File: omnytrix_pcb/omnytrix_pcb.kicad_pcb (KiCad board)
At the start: 2 copper layers, 38 x 45.5 mm, 17 parts, among them U1 LD3985M33R_SOT23, U3 STM32F411RCTx

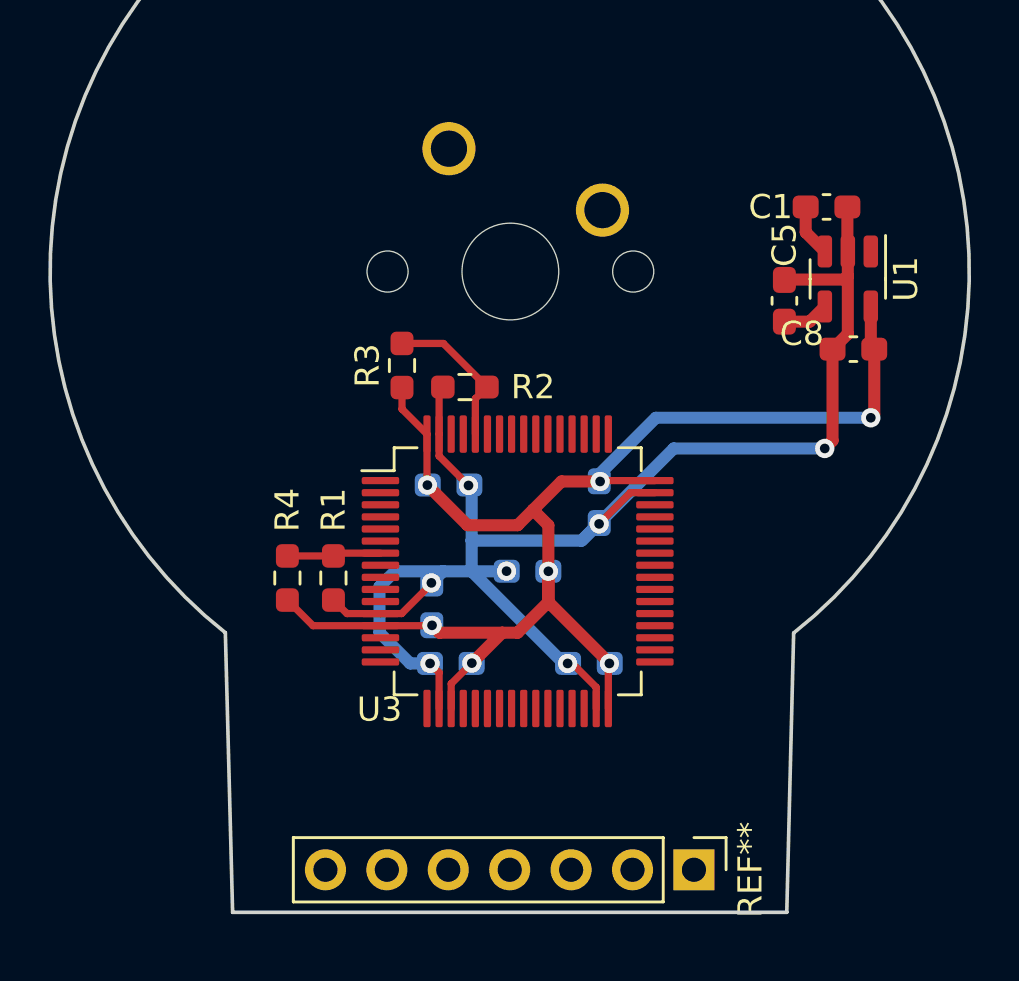
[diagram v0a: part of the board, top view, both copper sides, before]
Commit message: add some R and change position of components
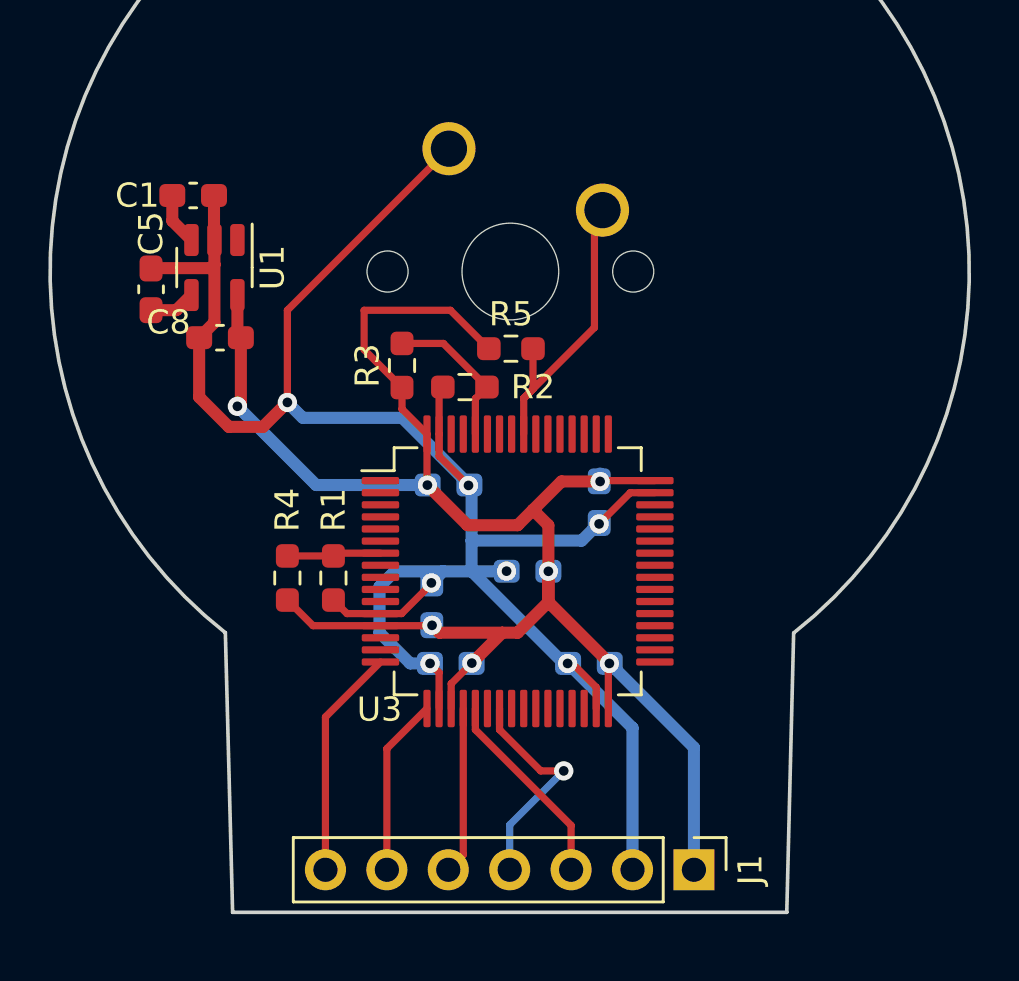
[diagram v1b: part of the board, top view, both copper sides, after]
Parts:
- removed REF**: PinHeader_1x07_P2.54mm_Vertical, Connector_PinHeader_2.54mm:PinHeader_1x07_P2.54mm_Vertical
- removed REF**: SW_Cherry_MX_1.00u_PCB, Button_Switch_Keyboard:SW_Cherry_MX_1.00u_PCB
- added J1: Conn_01x07, Connector_PinHeader_2.54mm:PinHeader_1x07_P2.54mm_Vertical, F.Cu at (107.6, 124.7)
- added R5: 10k, Resistor_SMD:R_0603_1608Metric_Pad0.98x0.95mm_HandSolder, F.Cu at (100.1, 103.2)
- added SW1: SW_Push, Button_Switch_Keyboard:SW_Cherry_MX_1.00u_PCB, B.Cu at (97.5, 94.9)
- moved C1 26.2 mm to (86.9, 96.9)
- moved C5 26.2 mm to (85.2, 100.7)
- moved C8 26.2 mm to (88.0, 102.7)
- moved U1 26.2 mm to (87.8, 99.8)
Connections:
- U3 pad 16: unconnected-(U3-PA2-Pad16) -> /RST
- U3 pad 17: unconnected-(U3-PA3-Pad17) -> /CS
- U3 pad 20: unconnected-(U3-PA4-Pad20) -> /DC
- U3 pad 21: unconnected-(U3-PA5-Pad21) -> /SCL
- U3 pad 23: unconnected-(U3-PA7-Pad23) -> /SDA
- U3 pad 36: unconnected-(U3-PB15-Pad36) -> /SD_CK
- U3 pad 39: unconnected-(U3-PC8-Pad39) -> /SD_D0
- U3 pad 40: unconnected-(U3-PC9-Pad40) -> /SD_D1
- U3 pad 42: unconnected-(U3-PA9-Pad42) -> /SD_D2
- U3 pad 52: unconnected-(U3-PC11-Pad52) -> /SD_D3
- U3 pad 54: unconnected-(U3-PD2-Pad54) -> /SD_CMD
- U3 pad 56: unconnected-(U3-PB4-Pad56) -> /BTN
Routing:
- net GND: track 67.0 -> 90.0 mm
- net +3.3V: track 59.2 -> 75.9 mm
- net /BTN: track 0.00 -> 12.9 mm
- net /RST: track 0.00 -> 9.54 mm
- net /SDA: track 0.00 -> 9.25 mm, vias 0 -> 1
- net /SCL: track 0.00 -> 8.31 mm
- net /CS: track 0.00 -> 7.36 mm
- net /DC: track 0.00 -> 6.93 mm

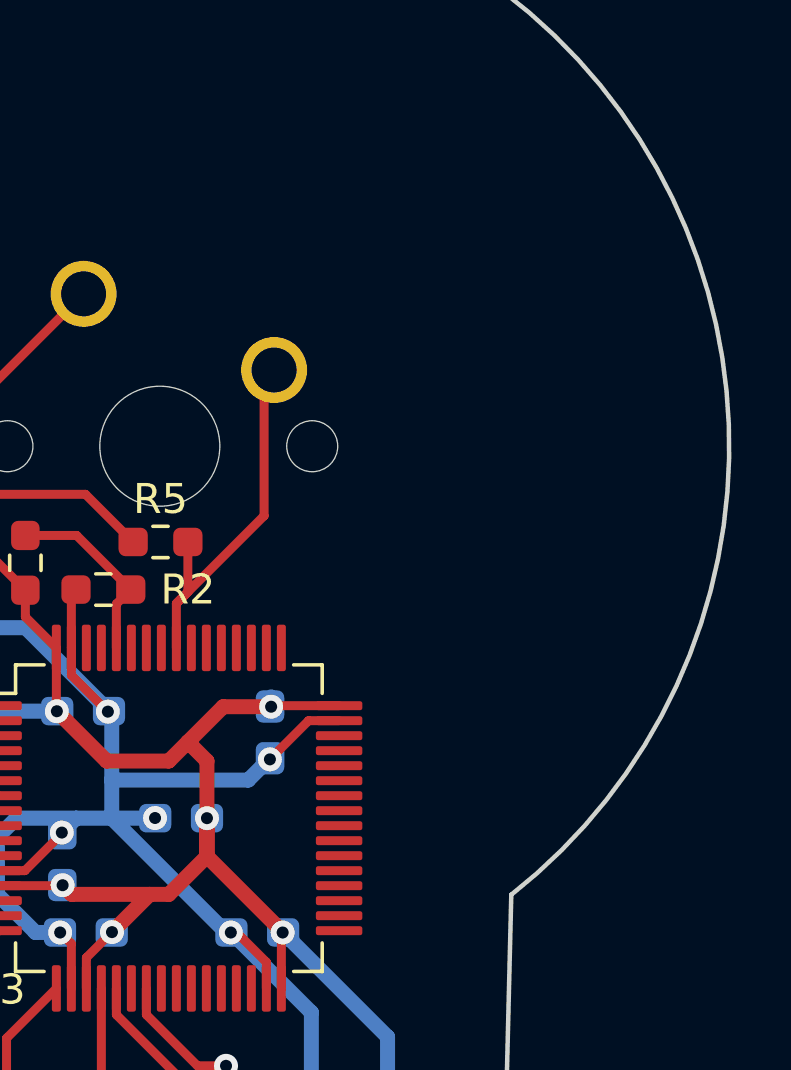
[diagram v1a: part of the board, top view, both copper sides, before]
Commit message: add microsd
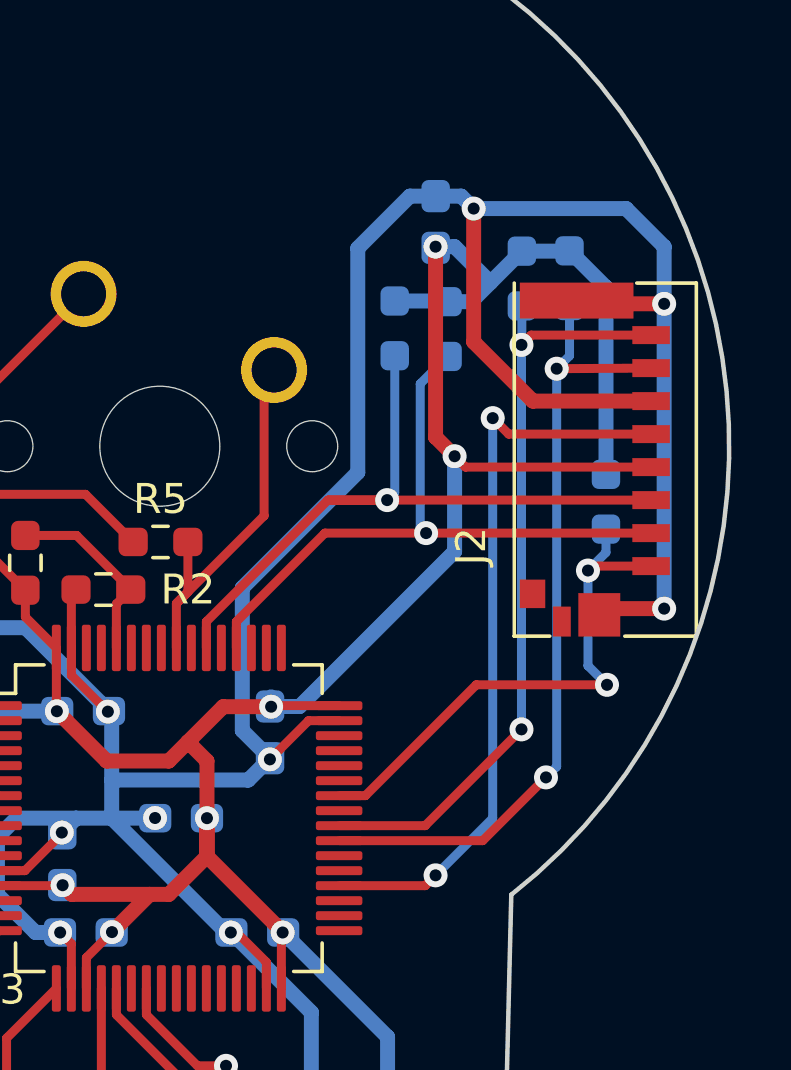
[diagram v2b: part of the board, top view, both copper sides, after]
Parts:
- added C10: 100nF, Capacitor_SMD:C_0603_1608Metric_Pad1.08x0.95mm_HandSolder, B.Cu at (109.2, 92.5)
- added J2: Micro_SD_Card_Det2, libs:microSD_molex, F.Cu at (118.0, 94.4)
- added R10: 47k, Resistor_SMD:R_0603_1608Metric_Pad0.98x0.95mm_HandSolder, B.Cu at (107.9, 96.1)
- added R6: 47k, Resistor_SMD:R_0603_1608Metric_Pad0.98x0.95mm_HandSolder, B.Cu at (112.1, 94.4)
- added R7: 47k, Resistor_SMD:R_0603_1608Metric_Pad0.98x0.95mm_HandSolder, B.Cu at (113.7, 94.4)
- added R8: 47k, Resistor_SMD:R_0603_1608Metric_Pad0.98x0.95mm_HandSolder, B.Cu at (109.6, 96.1)
- added R9: 47k, Resistor_SMD:R_0603_1608Metric_Pad0.98x0.95mm_HandSolder, B.Cu at (114.9, 101.8)
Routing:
- net GND: track 90.0 -> 149.0 mm, vias 7 -> 10
- net +3.3V: track 75.9 -> 118.2 mm, vias 7 -> 9
- net /SD_D0: track 0.00 -> 27.0 mm, vias 0 -> 2
- net /SD_D1: track 0.00 -> 26.0 mm, vias 0 -> 2
- net /SD_CK: track 0.00 -> 24.9 mm, vias 0 -> 2
- net /SD_CMD: track 0.00 -> 24.3 mm, vias 0 -> 1
- net /SD_D3: track 0.00 -> 22.3 mm, vias 0 -> 1
- net /SD_D2: track 0.00 -> 18.3 mm, vias 0 -> 2

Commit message: compare topor and my trace
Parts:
- added C1: 1mkF, Capacitor_SMD:C_0603_1608Metric_Pad1.08x0.95mm_HandSolder, F.Cu at (147.5, 96.7)
- added C10: 100nF, Capacitor_SMD:C_0603_1608Metric_Pad1.08x0.95mm_HandSolder, B.Cu at (169.8, 92.4)
- added C2: 10mkF, Capacitor_SMD:C_0603_1608Metric_Pad1.08x0.95mm_HandSolder, B.Cu at (161.4, 112.3)
- added C3: 100nF, Capacitor_SMD:C_0603_1608Metric_Pad1.08x0.95mm_HandSolder, B.Cu at (158.1, 108.7)
- added C4: 100nF, Capacitor_SMD:C_0603_1608Metric_Pad1.08x0.95mm_HandSolder, B.Cu at (164.3, 109.4)
- added C5: byp10nF, Capacitor_SMD:C_0603_1608Metric_Pad1.08x0.95mm_HandSolder, F.Cu at (145.8, 100.6)
- added C6: 100nF, Capacitor_SMD:C_0603_1608Metric_Pad1.08x0.95mm_HandSolder, B.Cu at (163.9, 116.1)
- added C7: 100nF, Capacitor_SMD:C_0603_1608Metric_Pad1.08x0.95mm_HandSolder, B.Cu at (157.4, 113.6)
- added C8: 1mkF, Capacitor_SMD:C_0603_1608Metric_Pad1.08x0.95mm_HandSolder, F.Cu at (148.6, 102.6)
- added C9: 100nF, Capacitor_SMD:C_0603_1608Metric_Pad1.08x0.95mm_HandSolder, B.Cu at (158.2, 116.1)
- added J1: Conn_01x07, Connector_PinHeader_2.54mm:PinHeader_1x07_P2.54mm_Vertical, F.Cu at (168.2, 124.6)
- added J2: Micro_SD_Card_Det2, libs:microSD_molex, F.Cu at (178.7, 94.3)
- added R1: 100k, Resistor_SMD:R_0603_1608Metric_Pad0.98x0.95mm_HandSolder, F.Cu at (153.3, 112.5)
- added R10: 47k, Resistor_SMD:R_0603_1608Metric_Pad0.98x0.95mm_HandSolder, B.Cu at (168.5, 95.9)
- added R2: 100k, Resistor_SMD:R_0603_1608Metric_Pad0.98x0.95mm_HandSolder, F.Cu at (158.8, 104.6)
- added R3: 10k, Resistor_SMD:R_0603_1608Metric_Pad0.98x0.95mm_HandSolder, F.Cu at (156.2, 103.7)
- added R4: 10k, Resistor_SMD:R_0603_1608Metric_Pad0.98x0.95mm_HandSolder, F.Cu at (151.4, 112.5)
- added R5: 10k, Resistor_SMD:R_0603_1608Metric_Pad0.98x0.95mm_HandSolder, F.Cu at (160.7, 103.1)
- added R6: 47k, Resistor_SMD:R_0603_1608Metric_Pad0.98x0.95mm_HandSolder, B.Cu at (172.7, 94.3)
- added R7: 47k, Resistor_SMD:R_0603_1608Metric_Pad0.98x0.95mm_HandSolder, B.Cu at (174.3, 94.3)
- added R8: 47k, Resistor_SMD:R_0603_1608Metric_Pad0.98x0.95mm_HandSolder, B.Cu at (170.2, 96.0)
- added R9: 47k, Resistor_SMD:R_0603_1608Metric_Pad0.98x0.95mm_HandSolder, B.Cu at (175.5, 101.7)
- added SW1: SW_Push, Button_Switch_Keyboard:SW_Cherry_MX_1.00u_PCB, B.Cu at (158.1, 94.8)
- added U1: LD3985M33R_SOT23, Package_TO_SOT_SMD:SOT-23-5, F.Cu at (148.4, 99.7)
- added U3: STM32F411RCTx, Package_QFP:LQFP-64_10x10mm_P0.5mm, F.Cu at (161.0, 112.3)
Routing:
- net +3.3V: track 118.2 -> 290.6 mm
- net GND: track 149.0 -> 314.0 mm
- net /SD_D2: track 18.3 -> 46.6 mm, vias 2 -> 3
- net /SD_D1: track 26.0 -> 49.2 mm, vias 2 -> 3
- net /SD_D0: track 27.0 -> 50.1 mm, vias 2 -> 3
- net /SD_CMD: track 24.3 -> 46.3 mm, vias 1 -> 3
- net /SD_D3: track 22.3 -> 43.1 mm, vias 1 -> 3
- net /SD_CK: track 24.9 -> 45.2 mm
- net /SCL: track 8.31 -> 20.0 mm
- net /BTN: track 12.9 -> 22.9 mm
- net /RST: track 9.54 -> 18.9 mm
- net BOOT0: track 6.40 -> 15.7 mm
- net /CS: track 7.36 -> 14.2 mm
- net /DC: track 6.93 -> 13.6 mm
- net /SDA: track 9.25 -> 15.9 mm
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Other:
- board size 38 x 45.5 mm -> 98.6 x 45.6 mm

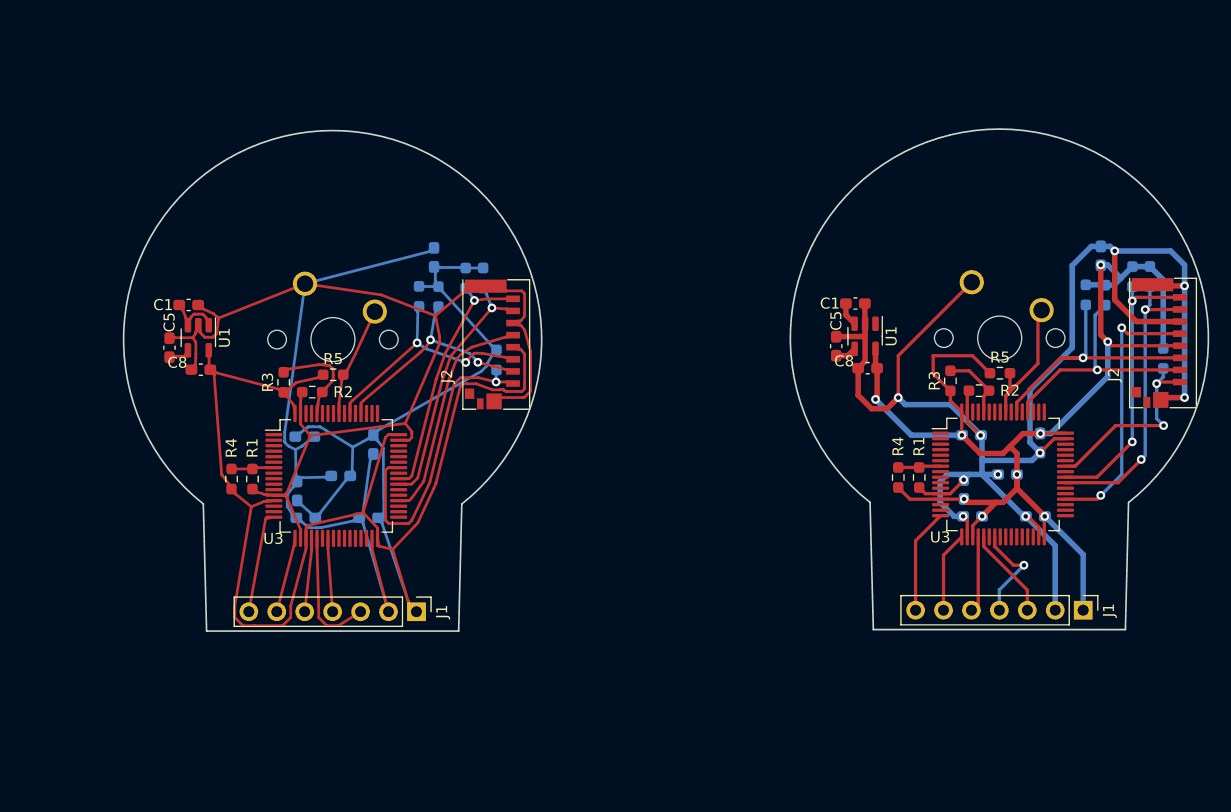
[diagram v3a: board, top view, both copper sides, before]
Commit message: add bat control
Add battery controller TP4056
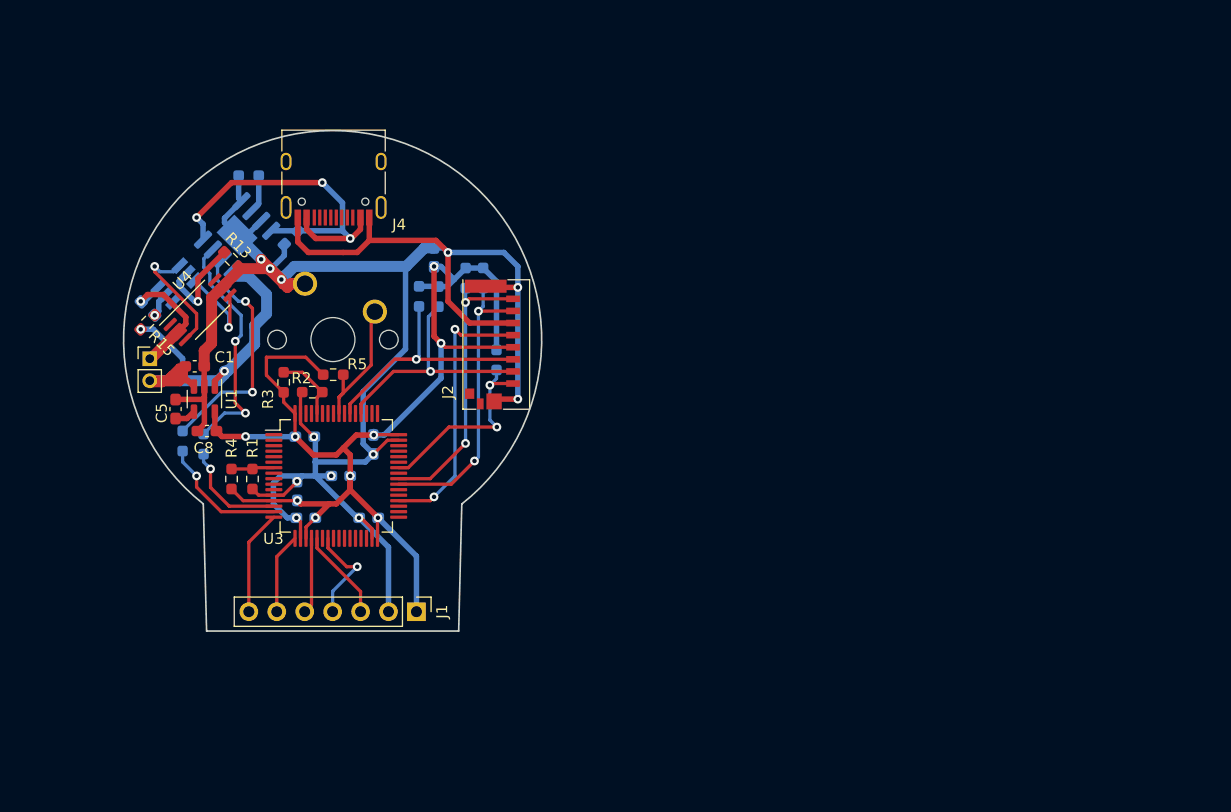
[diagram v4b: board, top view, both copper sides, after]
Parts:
- removed the C1 at (147.5, 96.7)
- removed the C10 at (169.8, 92.4)
- removed the C2 at (161.4, 112.3)
- removed the C3 at (158.1, 108.7)
- removed the C4 at (164.3, 109.4)
- removed the C5 at (145.8, 100.6)
- removed the C6 at (163.9, 116.1)
- removed the C7 at (157.4, 113.6)
- removed the C8 at (148.6, 102.6)
- removed the C9 at (158.2, 116.1)
- removed the J1 at (168.2, 124.6)
- removed the J2 at (178.7, 94.3)
- removed the R1 at (153.3, 112.5)
- removed the R10 at (168.5, 95.9)
- removed the R2 at (158.8, 104.6)
- removed the R3 at (156.2, 103.7)
- removed the R4 at (151.4, 112.5)
- removed the R5 at (160.7, 103.1)
- removed the R6 at (172.7, 94.3)
- removed the R7 at (174.3, 94.3)
- removed the R8 at (170.2, 96.0)
- removed the R9 at (175.5, 101.7)
- removed the SW1 at (158.1, 94.8)
- removed the U1 at (148.4, 99.7)
- removed the U3 at (161.0, 112.3)
- added C11: 100nF, Capacitor_SMD:C_0603_1608Metric_Pad1.08x0.95mm_HandSolder, B.Cu at (96.2, 90.7)
- added C12: 100nF, Capacitor_SMD:C_0603_1608Metric_Pad1.08x0.95mm_HandSolder, B.Cu at (83.2, 97.2)
- added J3: Conn_01x02, Connector_PinHeader_2.00mm:PinHeader_1x02_P2.00mm_Vertical, F.Cu at (83.4, 101.7)
- added J4: USB_C_Receptacle_PowerOnly_6P, Connector_USB:USB_C_Receptacle_HRO_TYPE-C-31-M-12, F.Cu at (100.1, 84.9)
- added R11: 47k, Resistor_SMD:R_0603_1608Metric_Pad0.98x0.95mm_HandSolder, B.Cu at (86.4, 109.2)
- added R12: 47k, Resistor_SMD:R_0603_1608Metric_Pad0.98x0.95mm_HandSolder, B.Cu at (88.3, 109.5)
- added R13: 1k, Resistor_SMD:R_0603_1608Metric_Pad0.98x0.95mm_HandSolder, F.Cu at (90.8, 92.7)
- added R14: 1.2k, Resistor_SMD:R_0603_1608Metric_Pad0.98x0.95mm_HandSolder, B.Cu at (92.4, 85.1)
- added R15: 100, Resistor_SMD:R_0603_1608Metric_Pad0.98x0.95mm_HandSolder, F.Cu at (83.2, 98.4)
- added U2: TP4056, Package_SO:SOIC-8-1EP_3.9x4.9mm_P1.27mm_EP2.29x3mm, B.Cu at (91.3, 90.5)
- added U4: FS8205A, Package_SO:TSSOP-8_4.4x3mm_P0.65mm, F.Cu at (87.9, 97.3)
- added U5: DW01, Package_TO_SOT_SMD:SOT-23-6_Handsoldering, B.Cu at (85.8, 94.9)
- C1: value 1mkF -> 10mkF
- moved C5 5.61 mm to (85.7, 106.3)
- moved C1 5.61 mm to (87.5, 102.4)
- moved C8 5.61 mm to (88.6, 108.3)
- moved U1 5.61 mm to (88.3, 105.4)
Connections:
- net +5V renamed +BATT
- U3 pad 14: unconnected-(U3-PA0-Pad14) -> /CHRG
- U3 pad 15: unconnected-(U3-PA1-Pad15) -> /STDBY
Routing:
- net +3.3V: track 290.6 -> 113.6 mm
- net GND: track 314.0 -> 193.7 mm, vias 10 -> 12
- net +BATT: track 7.34 -> 47.7 mm, vias 0 -> 2
- net +5V: track 0.00 -> 35.4 mm, vias 0 -> 3
- net /SD_D2: track 46.6 -> 18.3 mm, vias 3 -> 2
- net /SD_D1: track 49.2 -> 26.0 mm, vias 3 -> 2
- net /SD_D0: track 50.1 -> 27.0 mm, vias 3 -> 2
- net /SD_CMD: track 46.3 -> 24.3 mm, vias 3 -> 1
- net Net-(U2-~{CHRG}): track 0.00 -> 21.8 mm, vias 0 -> 2
- net Net-(U2-~{STDBY}): track 0.00 -> 21.8 mm, vias 0 -> 2
- net /SD_D3: track 43.1 -> 22.3 mm, vias 3 -> 1
- net /SD_CK: track 45.2 -> 24.9 mm
- net -BATT: track 0.00 -> 12.7 mm, vias 0 -> 1
- net /STDBY: track 0.00 -> 11.8 mm, vias 0 -> 1
- net /SCL: track 20.0 -> 8.31 mm
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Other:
- board size 98.6 x 45.6 mm -> 38 x 45.5 mm
- board text added: "+"
